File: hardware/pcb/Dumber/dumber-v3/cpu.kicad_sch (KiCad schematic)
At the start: 26 parts, among them J1 Conn_02x03_Odd_Even, J2 Conn_02x03_Odd_Even, J3 Conn_02x05_Odd_Even, J4 TE 1-84982-0, M1 Motor, M2 Motor, Q2 PMN52XP, U1 XBEE-3, U2 STM32F071CBTx, U7 A3909

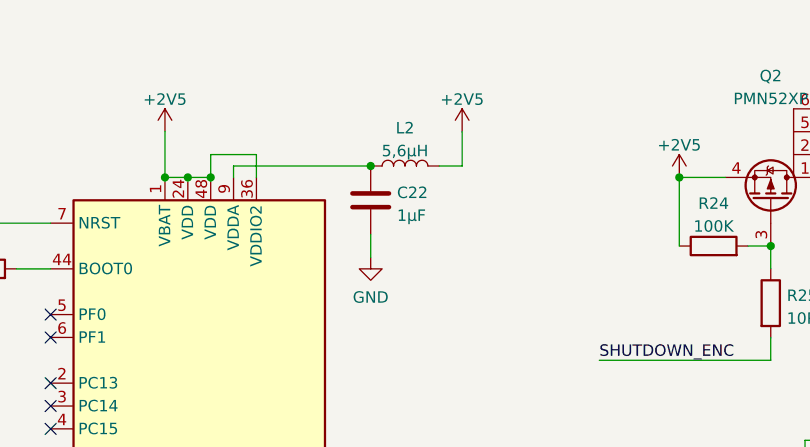
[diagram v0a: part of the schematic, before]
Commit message: Corrections autour des zones a activer ou deactiver en fonction de l'etat de connexion
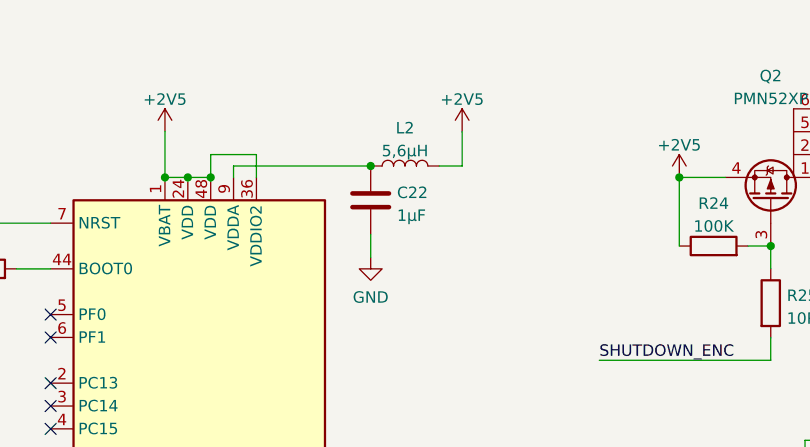
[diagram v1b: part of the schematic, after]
